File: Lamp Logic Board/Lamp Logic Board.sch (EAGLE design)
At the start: 44 parts, among them U1 ESP32-WROVER-IB, U2 SN74HCT245DWR, U3 LM1117MP-1.8, U4 LM50, U6 MSGEQ7DIL

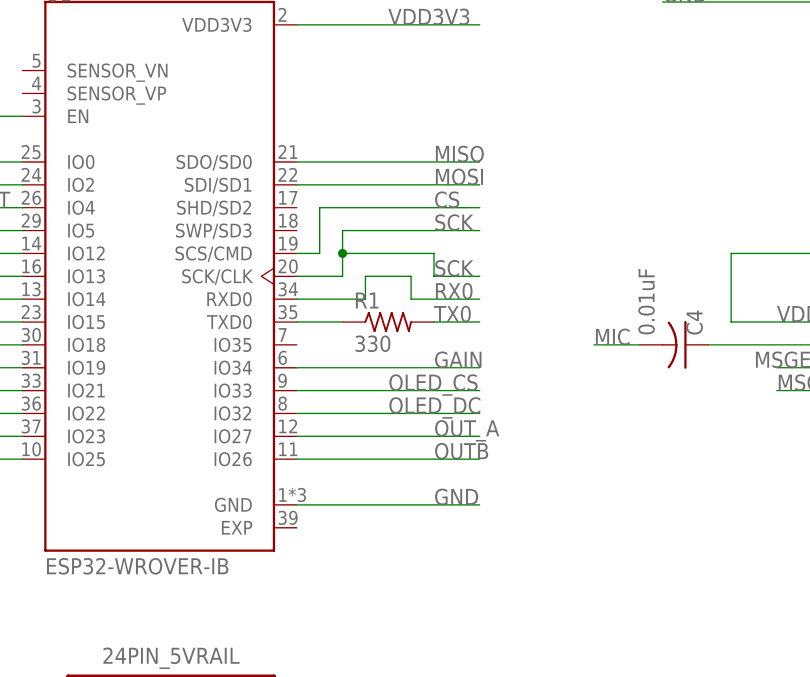
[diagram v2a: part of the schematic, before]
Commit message: Add files via upload
Added connection for MSGEQ7 as well direct connections to MIC output.
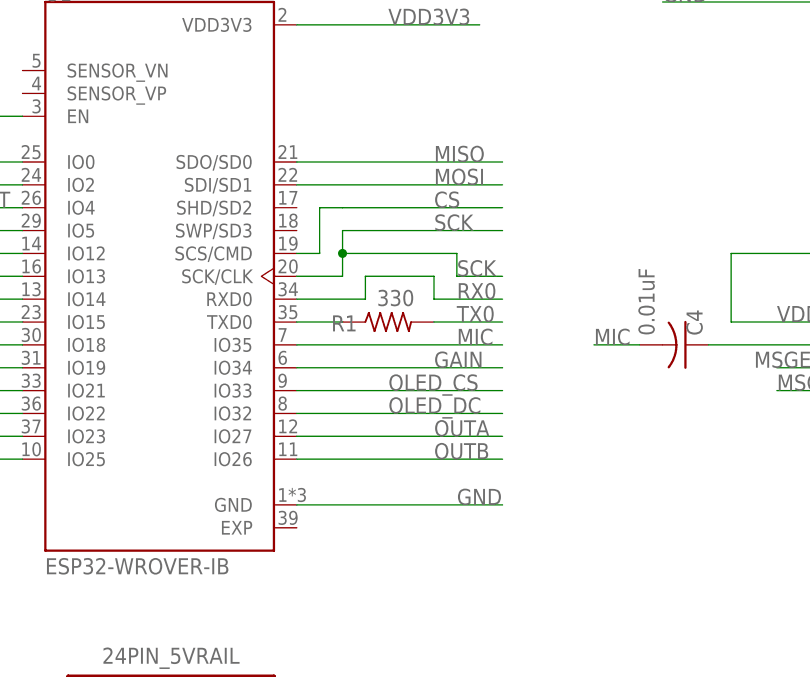
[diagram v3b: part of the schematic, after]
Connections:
- removed net OUT_A: U1.IO27
- net MIC: now also U1.IO35
- net OUTA: now also U1.IO27
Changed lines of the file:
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@@
 </instance>
 <instance part="R1" gate="G$1" x="236.22" y="132.08" smashed="yes">
-<attribute name="NAME" x="232.41" y="133.5786" size="1.778" layer="95"/>
-<attribute name="VALUE" x="232.41" y="128.778" size="1.778" layer="96"/>
+<attribute name="NAME" x="229.87" y="131.0386" size="1.778" layer="95"/>
+<attribute name="VALUE" x="234.95" y="133.858" size="1.778" layer="96"/>
 </instance>
 <instance part="R10" gate="G$1" x="119.38" y="93.98" smashed="yes">
@@
 <segment>
 <pinref part="U1" gate="G$1" pin="GND"/>
-<wire x1="226.06" y1="111.76" x2="246.38" y2="111.76" width="0.1524" layer="91"/>
-<label x="241.3" y="111.76" size="1.778" layer="95"/>
+<wire x1="226.06" y1="111.76" x2="248.92" y2="111.76" width="0.1524" layer="91"/>
+<label x="243.84" y="111.76" size="1.778" layer="95"/>
 </segment>
 <segment>
@@
 <wire x1="226.06" y1="134.62" x2="233.68" y2="134.62" width="0.1524" layer="91"/>
 <wire x1="233.68" y1="134.62" x2="233.68" y2="137.16" width="0.1524" layer="91"/>
-<wire x1="233.68" y1="137.16" x2="238.76" y2="137.16" width="0.1524" layer="91"/>
-<wire x1="238.76" y1="137.16" x2="238.76" y2="134.62" width="0.1524" layer="91"/>
-<wire x1="238.76" y1="134.62" x2="246.38" y2="134.62" width="0.1524" layer="91"/>
-<label x="241.3" y="134.62" size="1.778" layer="95"/>
+<wire x1="233.68" y1="137.16" x2="241.3" y2="137.16" width="0.1524" layer="91"/>
+<wire x1="241.3" y1="137.16" x2="241.3" y2="134.62" width="0.1524" layer="91"/>
+<wire x1="241.3" y1="134.62" x2="248.92" y2="134.62" width="0.1524" layer="91"/>
+<label x="243.84" y="134.62" size="1.778" layer="95"/>
 </segment>
 <segment>
@@
 <net name="TX0" class="0">
 <segment>
-<wire x1="241.3" y1="132.08" x2="246.38" y2="132.08" width="0.1524" layer="91"/>
-<label x="241.3" y="132.08" size="1.778" layer="95"/>
+<wire x1="241.3" y1="132.08" x2="248.92" y2="132.08" width="0.1524" layer="91"/>
+<label x="243.84" y="132.08" size="1.778" layer="95"/>
 <pinref part="R1" gate="G$1" pin="2"/>
 </segment>
@@
 <wire x1="226.06" y1="137.16" x2="231.14" y2="137.16" width="0.1524" layer="91"/>
 <wire x1="231.14" y1="137.16" x2="231.14" y2="139.7" width="0.1524" layer="91"/>
-<wire x1="231.14" y1="139.7" x2="241.3" y2="139.7" width="0.1524" layer="91"/>
-<wire x1="241.3" y1="139.7" x2="241.3" y2="137.16" width="0.1524" layer="91"/>
-<wire x1="241.3" y1="137.16" x2="246.38" y2="137.16" width="0.1524" layer="91"/>
-<label x="241.3" y="137.16" size="1.778" layer="95"/>
+<wire x1="231.14" y1="139.7" x2="243.84" y2="139.7" width="0.1524" layer="91"/>
+<wire x1="243.84" y1="139.7" x2="243.84" y2="137.16" width="0.1524" layer="91"/>
+<wire x1="243.84" y1="137.16" x2="248.92" y2="137.16" width="0.1524" layer="91"/>
+<label x="243.84" y="137.16" size="1.778" layer="95"/>
 <wire x1="231.14" y1="139.7" x2="231.14" y2="142.24" width="0.1524" layer="91"/>
-<wire x1="231.14" y1="142.24" x2="246.38" y2="142.24" width="0.1524" layer="91"/>
+<wire x1="231.14" y1="142.24" x2="248.92" y2="142.24" width="0.1524" layer="91"/>
 <junction x="231.14" y="139.7"/>
 <label x="241.3" y="142.24" size="1.778" layer="95"/>
@@
 <pinref part="C4" gate="G$1" pin="2"/>
 </segment>
+<segment>
+<pinref part="U1" gate="G$1" pin="IO35"/>
+<wire x1="226.06" y1="129.54" x2="248.92" y2="129.54" width="0.1524" layer="91"/>
+<label x="243.84" y="129.54" size="1.778" layer="95"/>
+</segment>
 </net>
 <net name="GAIN" class="0">
@@
 <segment>
 <pinref part="U1" gate="G$1" pin="IO34"/>
-<wire x1="226.06" y1="127" x2="246.38" y2="127" width="0.1524" layer="91"/>
+<wire x1="226.06" y1="127" x2="248.92" y2="127" width="0.1524" layer="91"/>
 <label x="241.3" y="127" size="1.778" layer="95"/>
 </segment>
@@
 <segment>
 <pinref part="U1" gate="G$1" pin="SDI/SD1"/>
-<wire x1="226.06" y1="147.32" x2="246.38" y2="147.32" width="0.1524" layer="91"/>
+<wire x1="226.06" y1="147.32" x2="248.92" y2="147.32" width="0.1524" layer="91"/>
 <label x="241.3" y="147.32" size="1.778" layer="95"/>
 </segment>
@@
 <segment>
 <pinref part="U1" gate="G$1" pin="SDO/SD0"/>
-<wire x1="226.06" y1="149.86" x2="246.38" y2="149.86" width="0.1524" layer="91"/>
+<wire x1="226.06" y1="149.86" x2="248.92" y2="149.86" width="0.1524" layer="91"/>
 <label x="241.3" y="149.86" size="1.778" layer="95"/>
 </segment>
@@
 <wire x1="226.06" y1="139.7" x2="228.6" y2="139.7" width="0.1524" layer="91"/>
 <wire x1="228.6" y1="139.7" x2="228.6" y2="144.78" width="0.1524" layer="91"/>
-<wire x1="228.6" y1="144.78" x2="246.38" y2="144.78" width="0.1524" layer="91"/>
+<wire x1="228.6" y1="144.78" x2="231.14" y2="144.78" width="0.1524" layer="91"/>
+<wire x1="231.14" y1="144.78" x2="248.92" y2="144.78" width="0.1524" layer="91"/>
 <label x="241.3" y="144.78" size="1.778" layer="95"/>
 </segment>
@@
 <pinref part="C8" gate="G$1" pin="1"/>
 </segment>
+<segment>
+<pinref part="U1" gate="G$1" pin="IO27"/>
+<wire x1="226.06" y1="119.38" x2="248.92" y2="119.38" width="0.1524" layer="91"/>
+<label x="241.3" y="119.38" size="1.778" layer="95"/>
+</segment>
 </net>
 <net name="OUTB" class="0">
@@
 <segment>
 <pinref part="U1" gate="G$1" pin="IO26"/>
-<wire x1="226.06" y1="116.84" x2="246.38" y2="116.84" width="0.1524" layer="91"/>
+<wire x1="226.06" y1="116.84" x2="248.92" y2="116.84" width="0.1524" layer="91"/>
 <label x="241.3" y="116.84" size="1.778" layer="95"/>
 </segment>
@@
 <segment>
 <pinref part="U1" gate="G$1" pin="IO33"/>
-<wire x1="226.06" y1="124.46" x2="246.38" y2="124.46" width="0.1524" layer="91"/>
+<wire x1="226.06" y1="124.46" x2="248.92" y2="124.46" width="0.1524" layer="91"/>
 <label x="236.22" y="124.46" size="1.778" layer="95"/>
 </segment>
@@
 <segment>
 <pinref part="U1" gate="G$1" pin="IO32"/>
-<wire x1="226.06" y1="121.92" x2="246.38" y2="121.92" width="0.1524" layer="91"/>
+<wire x1="226.06" y1="121.92" x2="248.92" y2="121.92" width="0.1524" layer="91"/>
 <label x="236.22" y="121.92" size="1.778" layer="95"/>
 </segment>
@@
 </segment>
 </net>
-<net name="OUT_A" class="0">
-<segment>
-<pinref part="U1" gate="G$1" pin="IO27"/>
-<wire x1="226.06" y1="119.38" x2="246.38" y2="119.38" width="0.1524" layer="91"/>
-<label x="241.3" y="119.38" size="1.778" layer="95"/>
-</segment>
-</net>

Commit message: Add files via upload
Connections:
- net GND: now also U1.EXP
- net MIC: now also U1.SENSOR_VN; no longer U1.IO35
- net MSGEQ_STROBE: now also U1.IO35
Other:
- moved on the sheet: 24PIN_5VRAIL, 24PIN_DATARAIL, 24PIN_GNDRAIL, C1, C10, C2, C3, C4, C6, C7, C8, C9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

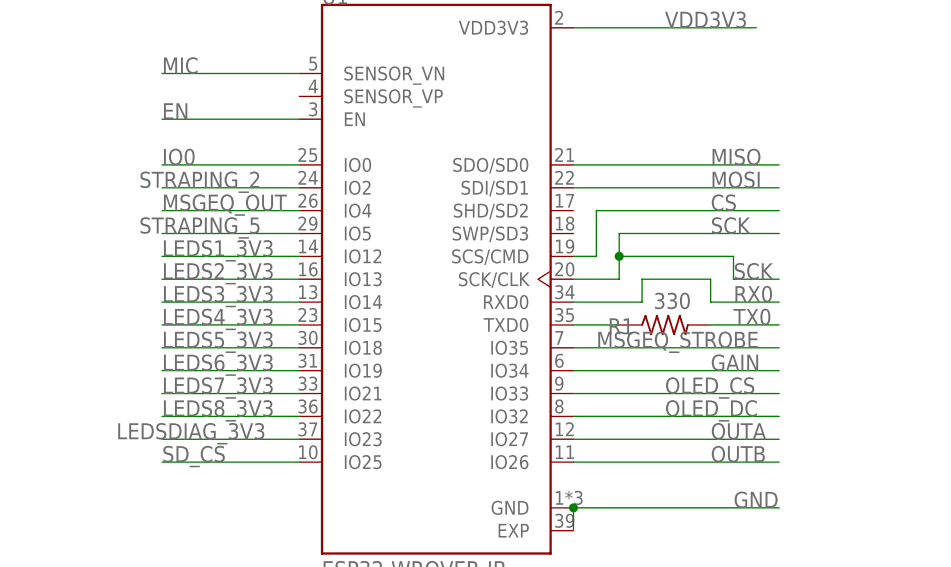
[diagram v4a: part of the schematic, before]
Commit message: Add files via upload
Uploading a version, that does not have a messed up board file.
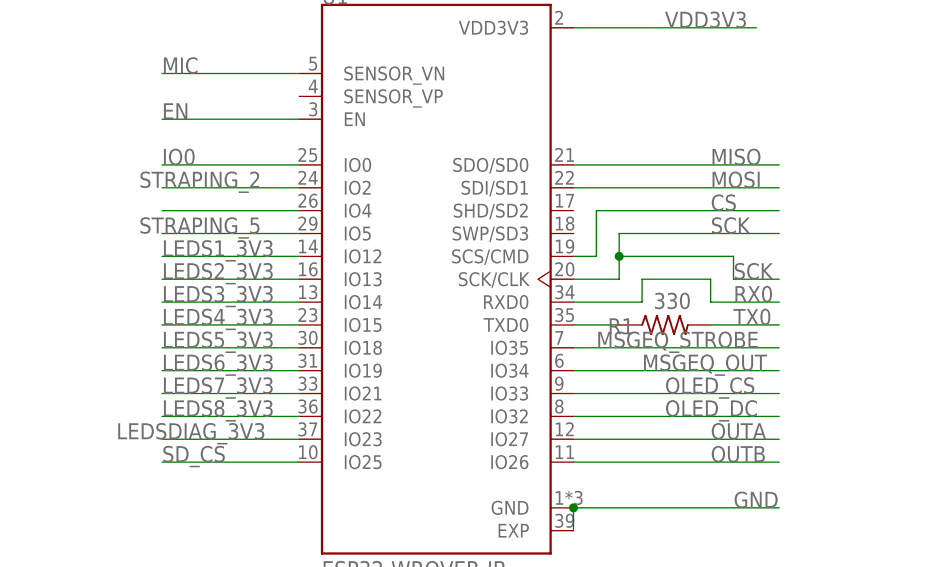
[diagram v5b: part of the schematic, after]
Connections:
- new net N$5: U1.IO4
- net GAIN: no longer U1.IO34
- net MSGEQ_OUT: now also U1.IO34; no longer U1.IO4
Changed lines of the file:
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@@
 <label x="441.96" y="121.92" size="1.778" layer="95"/>
-</segment>
-<segment>
-<pinref part="U1" gate="G$1" pin="IO34"/>
-<wire x1="210.82" y1="109.22" x2="233.68" y2="109.22" width="0.1524" layer="91"/>
-<label x="226.06" y="109.22" size="1.778" layer="95"/>
 </segment>
 </net>
@@
 </segment>
 <segment>
-<pinref part="U1" gate="G$1" pin="IO4"/>
-<wire x1="180.34" y1="127" x2="165.1" y2="127" width="0.1524" layer="91"/>
-<label x="165.1" y="127" size="1.778" layer="95"/>
+<pinref part="U1" gate="G$1" pin="IO34"/>
+<wire x1="210.82" y1="109.22" x2="233.68" y2="109.22" width="0.1524" layer="91"/>
+<label x="218.44" y="109.22" size="1.778" layer="95"/>
 </segment>
 </net>
@@
 </segment>
 </net>
+<net name="N$5" class="0">
+<segment>
+<pinref part="U1" gate="G$1" pin="IO4"/>
+<wire x1="180.34" y1="127" x2="165.1" y2="127" width="0.1524" layer="91"/>
+</segment>
+</net>

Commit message: It's the £2 one.
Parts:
- removed 24PIN_5VRAIL, 24PIN_DATARAIL, 24PIN_GNDRAIL: (no value), pinhead:PINHD-1X8
- removed OLED_CONN: (no value), pinhead:PINHD-1X7
- removed SERIAL_PORT, SPI_PORT: (no value), pinhead:PINHD-1X4
- added PAD5V1, PADGND1: (no value), wirepad:SMD5
- added R11: (no value), resistor:R-US_R0603
- added R16: 330, resistor:R-US_R1206
- added U$4: 3X8PINHEAD, 3X8PINHEAD:3X8PINHEAD
- added U$5: 2X4PINHEAD, 2X4PINHEAD:2X4PINHEAD
- added U5: SPIOLED_STANDOFF, SPIOLED-STANDOFF:SPIOLED_STANDOFF
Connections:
- removed net N$16: R3.1, U2.B2
- removed net N$17: R4.1, U2.B3
- removed net N$18: R5.1, U2.B4
- removed net N$19: R6.1, U2.B5
- removed net N$20: R7.1, U2.B6
- removed net N$21: R8.1, U2.B7
- removed net N$22: R9.1, U2.B8
- new net N$1: R9.1, U2.B1
- new net N$10: R7.1, U2.B3
- new net N$11: R6.1, U2.B4
- new net N$12: R5.1, U2.B5
- new net N$13: R4.1, U2.B6
- new net N$14: R3.1, U2.B7
- new net N$6: R8.1, U2.B2
- new net ROTARY_BUTTON_IN: R11.1, R16.2, U1.SENSOR_VP
- net CS: now also U$5.CS; no longer SPI_PORT.2
- net GND: now also PADGND1.P, U$2.4, U$4.1, U$4.2, U$4.3, U$4.4, U$4.5, U$4.6, U$4.7, U$4.8, U$5.GND, U5.GND; no longer 24PIN_GNDRAIL.1, 24PIN_GNDRAIL.2, 24PIN_GNDRAIL.3, 24PIN_GNDRAIL.4, 24PIN_GNDRAIL.5, 24PIN_GNDRAIL.6, 24PIN_GNDRAIL.7, 24PIN_GNDRAIL.8, OLED_CONN.1, SERIAL_PORT.1
- net LEDS1_3V3: now also U1.IO15; no longer U1.IO12
- net LEDS1_5V: now also U$4.9; no longer 24PIN_DATARAIL.1
- net LEDS2_3V3: now also U1.IO18; no longer U1.IO13
- net LEDS2_5V: now also U$4.10; no longer 24PIN_DATARAIL.2
- net LEDS3_3V3: now also U1.IO19; no longer U1.IO14
- net LEDS3_5V: now also U$4.11; no longer 24PIN_DATARAIL.3
- net LEDS4_3V3: now also U1.IO21; no longer U1.IO15
- net LEDS4_5V: now also U$4.12; no longer 24PIN_DATARAIL.4
- net LEDS5_3V3: now also U1.IO22; no longer U1.IO18
- net LEDS5_5V: now also U$4.13; no longer 24PIN_DATARAIL.5
- net LEDS6_3V3: now also U1.IO14; no longer U1.IO19
- net LEDS6_5V: now also U$4.14; no longer 24PIN_DATARAIL.6
- net LEDS7_3V3: now also U1.IO12; no longer U1.IO21
- net LEDS7_5V: now also U$4.15; no longer 24PIN_DATARAIL.7
- net LEDS8_3V3: now also U1.IO13; no longer U1.IO22
- net LEDS8_5V: now also U$4.16; no longer 24PIN_DATARAIL.8
- net MISO: now also U$5.MISO; no longer SPI_PORT.4
- net MOSI: now also U$5.MOSI, U5.DIN; no longer OLED_CONN.4, SPI_PORT.3
- net N$15: now also U2.B8; no longer U2.B1
- net N$5: now also R16.1, U$2.5; no longer U1.IO4
- net OLED_CS: now also U5.CS; no longer OLED_CONN.7
- net OLED_DC: now also U5.DC; no longer OLED_CONN.6
- net OLED_RESET: now also U5.RST; no longer OLED_CONN.5
- net OUTA: now also U1.IO26; no longer U1.IO27
- net OUTB: now also U1.IO27; no longer U1.IO26
- net RX0: now also U$5.RX0; no longer SERIAL_PORT.3
- net SCK: now also U$5.SCK, U5.CLK; no longer OLED_CONN.3, SPI_PORT.1
- net TX0: now also U$5.TX0; no longer SERIAL_PORT.4
- net VDD3V3: now also R11.2, U$5.VDD, U5.VCC; no longer OLED_CONN.2, SERIAL_PORT.2
- net VDD3V3_TEMP_OUT: now also U1.IO4
- net VDD5V: now also PAD5V1.P, U$4.17, U$4.18, U$4.19, U$4.20, U$4.21, U$4.22, U$4.23, U$4.24; no longer 24PIN_5VRAIL.1, 24PIN_5VRAIL.2, 24PIN_5VRAIL.3, 24PIN_5VRAIL.4, 24PIN_5VRAIL.5, 24PIN_5VRAIL.6, 24PIN_5VRAIL.7, 24PIN_5VRAIL.8
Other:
- moved on the sheet: R2, R3, R4, R5, R6, R7, R8, R9
